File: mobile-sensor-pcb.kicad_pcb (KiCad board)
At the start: 2 copper layers, 125.7 x 67.6 mm, 93 parts, among them J1 SMA, J2 USB_OTG, J3 JST PH, Q1 PNP-BJT-BIASED_SOT, SW1 RESET, SW2 ON/OFF, U1 3M_2908-05WB-MG, U10 LP2980AIM5-3.3/NOPB, U11 LP2980AIM5-3.3/NOPB, U12 LP2980AIM5-3.3/NOPB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

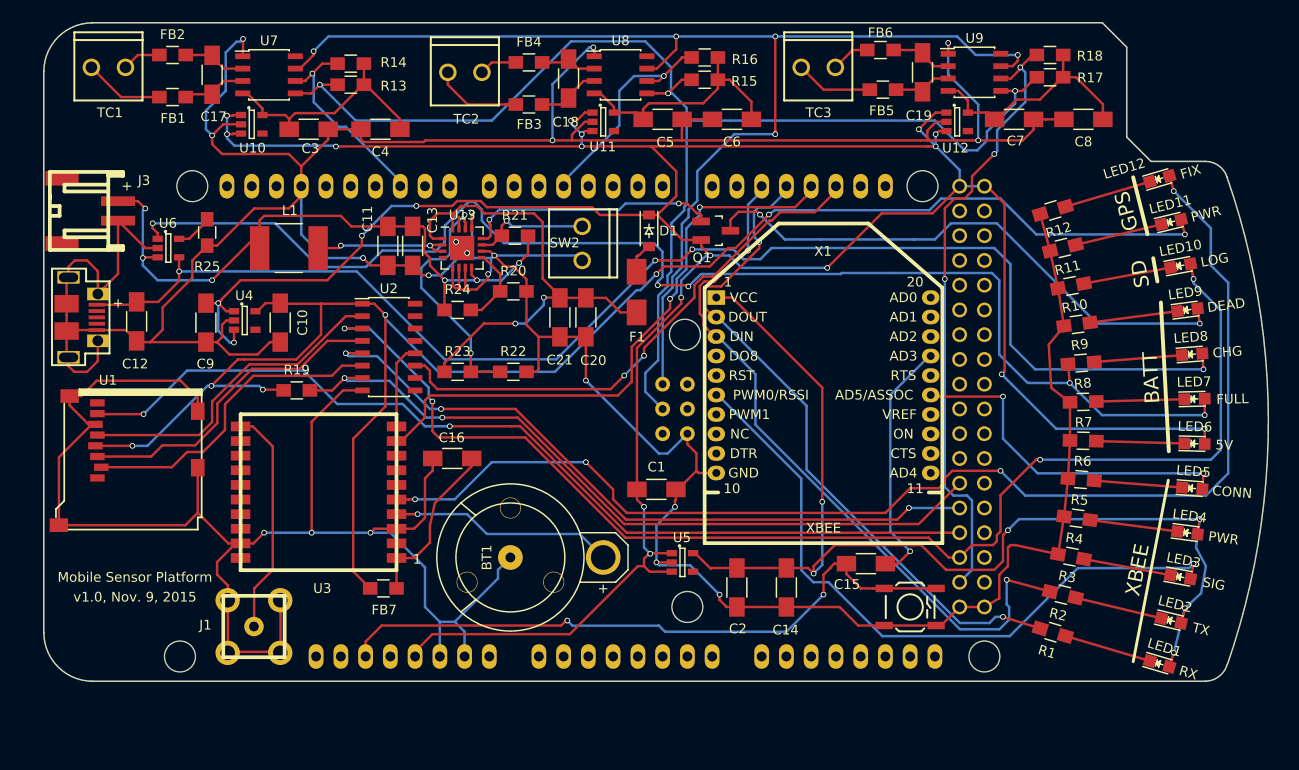
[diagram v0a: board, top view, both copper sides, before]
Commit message: Add BOMs and what appear to be some final PCB changes
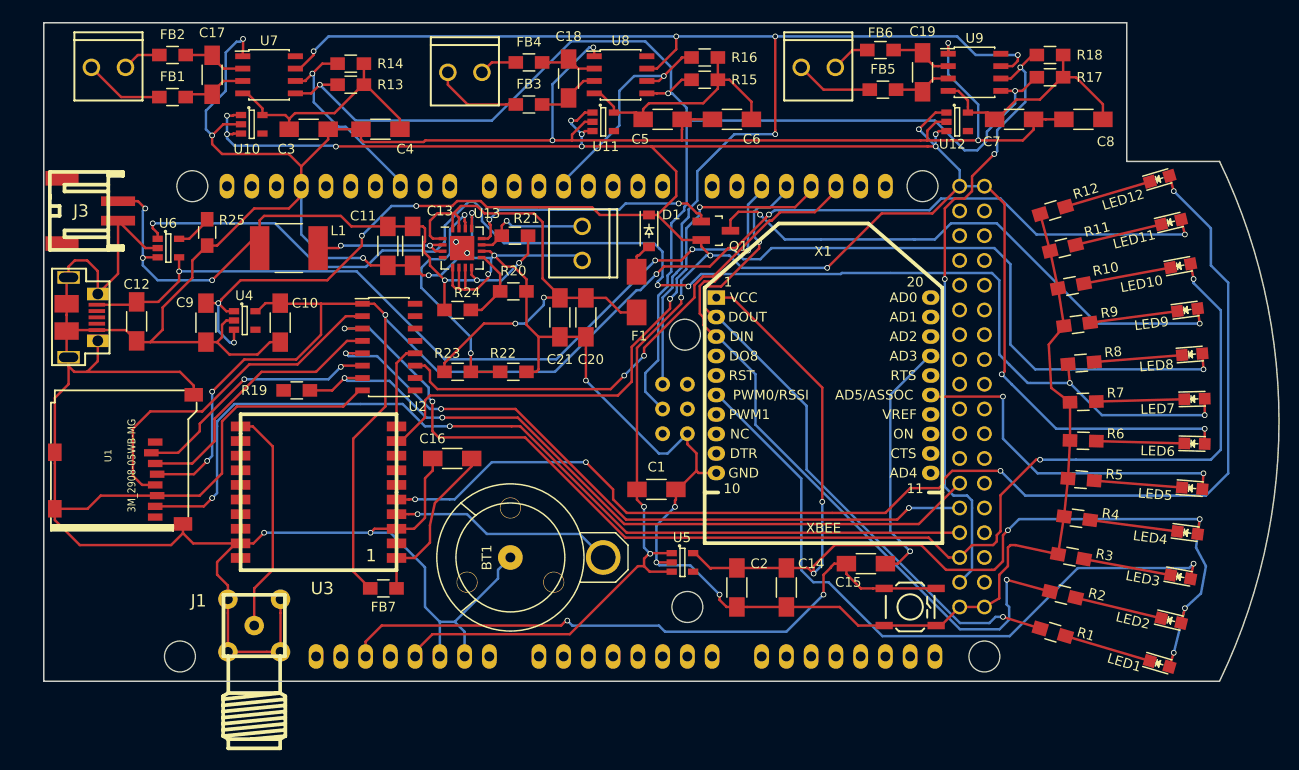
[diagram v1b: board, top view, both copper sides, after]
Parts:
- moved U1 6.98 mm to (62.2, 127.9), turned to 270 degrees
- moved J1 0.10 mm to (72.4, 146.7), turned to 180 degrees
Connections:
- R19 pad 1: GPS-SD-3V3 -> Net-(R19-Pad1)
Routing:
- net GND: track 604.6 -> 620.3 mm, vias 20 -> 19
- net GPS-SD-3V3: track 178.1 -> 169.3 mm, vias 7 -> 6
- net Net-(U1-Pad2): track 32.7 -> 25.8 mm, vias 0 -> 2
- net Net-(U1-Pad3): track 33.3 -> 27.8 mm
- net Net-(U1-Pad5): track 33.5 -> 35.8 mm
- net SD-MISO: track 97.2 -> 96.7 mm
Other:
- board size 125.7 x 67.6 mm -> 126.8 x 67.6 mm
- board text removed: "+"
- board text removed: "BATT"
- board text removed: "GPS"
- board text removed: "Mobile Sensor Platform"
- board text removed: "SD"
- board text removed: "XBEE"
- board text removed: "v1.0, Nov. 9, 2015"

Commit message: Fix a R19 connection, spin SD card holder, fix SMA jack
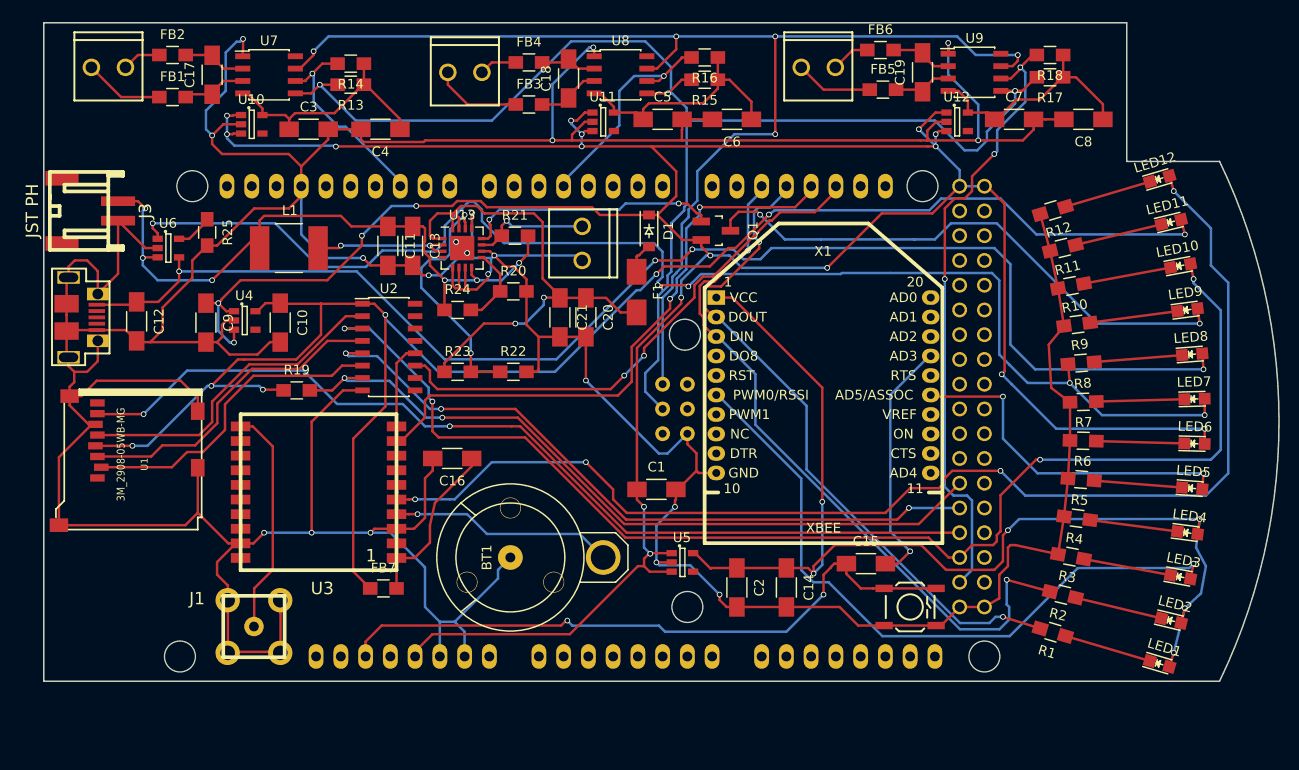
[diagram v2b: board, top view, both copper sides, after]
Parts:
- moved U1 6.98 mm to (56.3, 131.5), turned to 90 degrees
- moved J1 0.10 mm to (72.4, 146.8), turned to 0 degrees
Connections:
- R19 pad 1: Net-(R19-Pad1) -> GPS-SD-3V3
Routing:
- net GND: track 620.3 -> 607.3 mm, vias 19 -> 20
- net GPS-SD-3V3: track 169.3 -> 178.1 mm, vias 6 -> 7
- net Net-(U1-Pad2): track 25.8 -> 32.7 mm, vias 2 -> 0
- net Net-(U1-Pad3): track 27.8 -> 33.3 mm
- net Net-(U1-Pad5): track 35.8 -> 33.5 mm
- net SD-MISO: track 96.7 -> 97.2 mm

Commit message: Lots of little tweaks, rounding corners, fixing designators, adding labels, name, date and rev
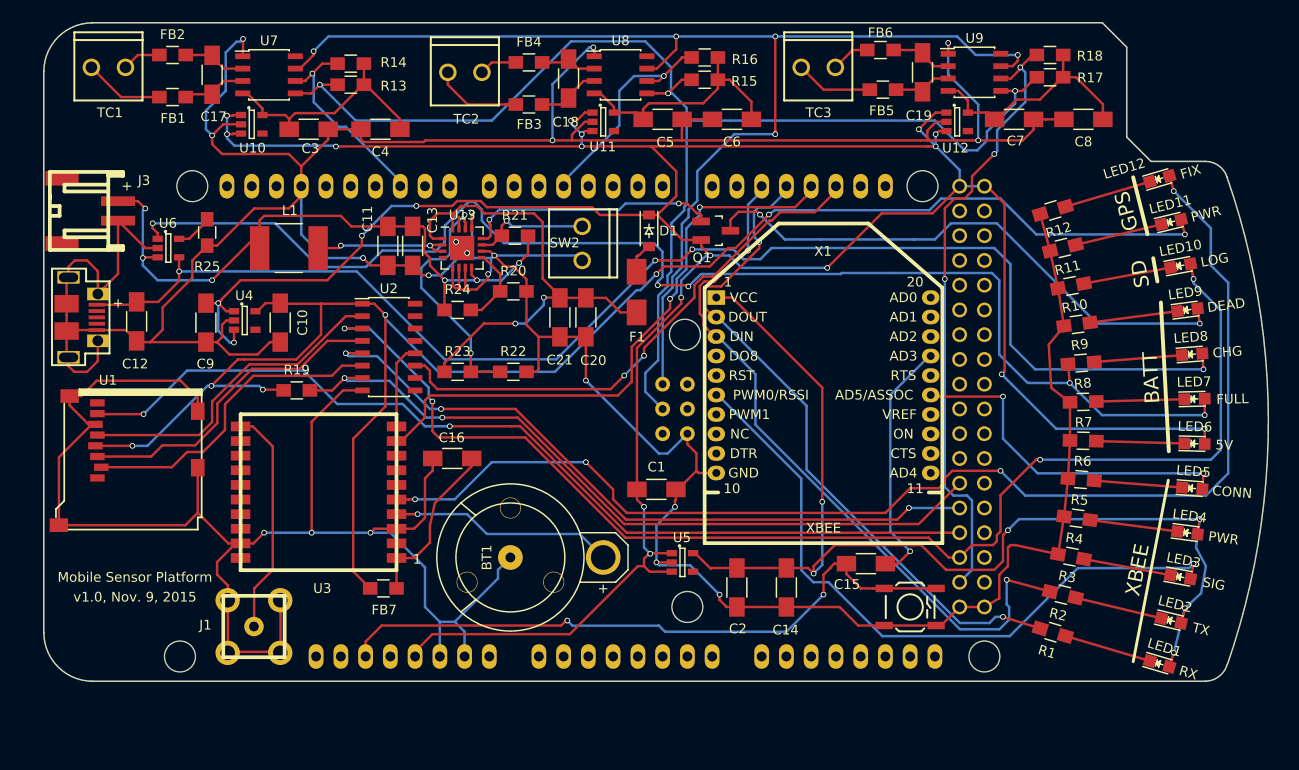
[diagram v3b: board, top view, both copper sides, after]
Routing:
- net GND: track 607.3 -> 604.6 mm
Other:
- board size 126.8 x 67.6 mm -> 125.7 x 67.6 mm
- board text added: "+"
- board text added: "BATT"
- board text added: "GPS"
- board text added: "Mobile Sensor Platform"
- board text added: "SD"
- board text added: "XBEE"
- board text added: "v1.0, Nov. 9, 2015"
